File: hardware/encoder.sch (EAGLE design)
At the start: 10 parts, among them Q1 BCP56, Q2 BCP53, Q3 IRF540

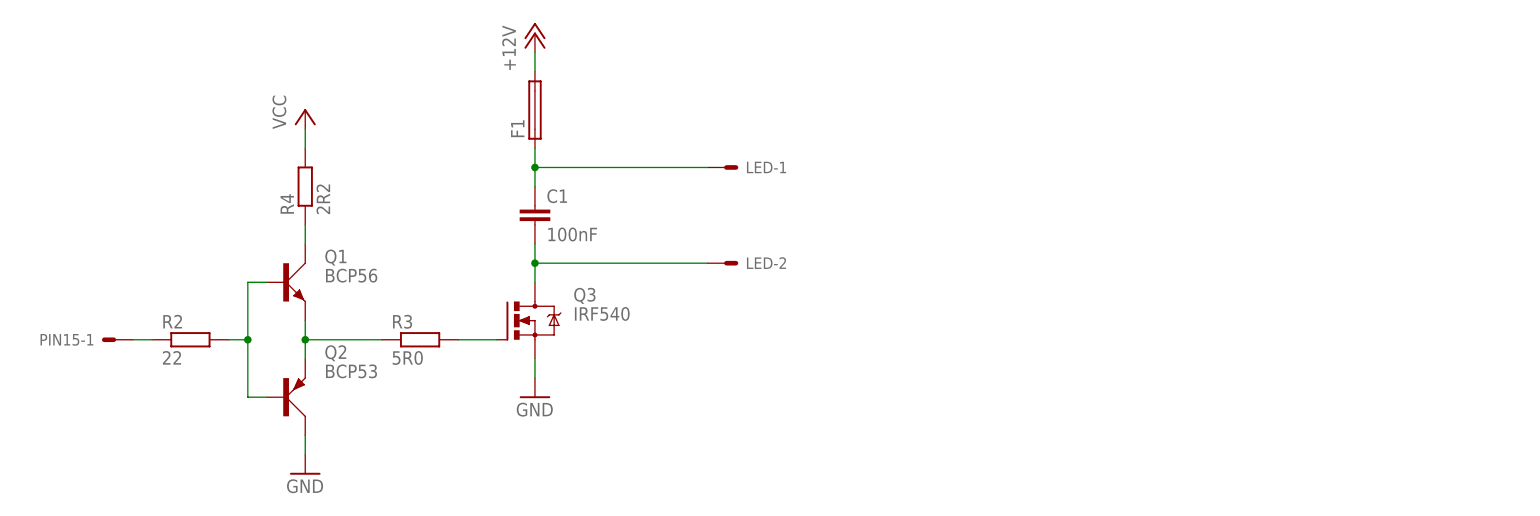
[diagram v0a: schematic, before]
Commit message: реорганизация
Разводка дочерней платы энкодера (теперь три платы в одном файле),
актуальная папка  для железа - hardware
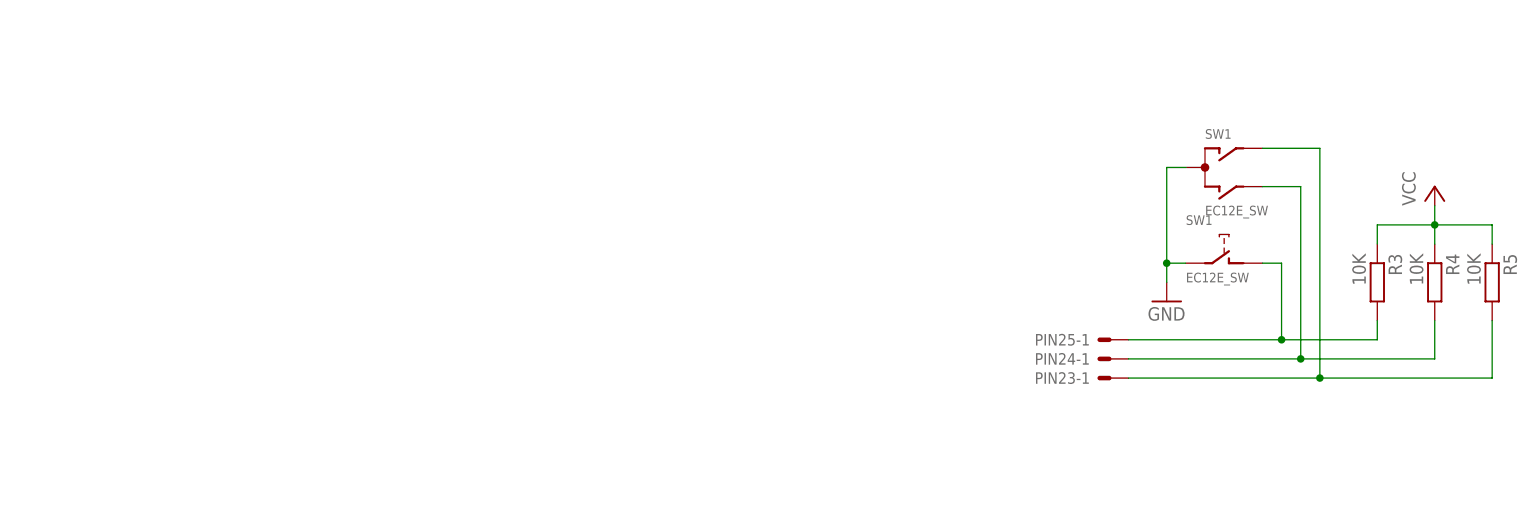
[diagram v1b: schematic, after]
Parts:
- removed C1: 100nF, capacitor-wima:C2,5-3
- removed F1: (no value), fuse:TE5
- removed LED, PIN15: 5566-10, con-molex:5566-10
- removed Q1: BCP56, transistor-small-signal:BC639
- removed Q2: BCP53, transistor-small-signal:BC640
- removed Q3: IRF540, transistor-power:IRF540
- removed R2: 22, resistor:R-EU_R1206
- added PIN23, PIN24, PIN25: 5566-10, con-molex:5566-10
- added R5: 10K, resistor:R-EU_M1206
- added SW1: EC12E_SW, switch-alps:EC12E_SW
- R3: value 5R0 -> 10K; device resistor:R-EU_R1206 -> resistor:R-EU_M1206
- R4: value 2R2 -> 10K; device resistor:R-EU_R1206 -> resistor:R-EU_M1206
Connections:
- removed net +12V: F1.2
- removed net N$12: Q1.C, R4.1
- removed net N$13: C1.1, F1.1, LED-1.S
- removed net N$6: PIN15-1.S, R2.1
- removed net N$8: Q1.E, Q2.E, R3.1
- net GND: now also SW1G$1.C, SW1G$2.2; no longer Q2.C, Q3.S
- net N$10: now also PIN25-1.S, R3.2, SW1G$2.1; no longer C1.2, LED-2.S, Q3.D
- net N$5: now also PIN23-1.S, R5.2, SW1G$1.A; no longer Q1.B, Q2.B, R2.2
- net N$9: now also PIN24-1.S, R4.2, SW1G$1.B; no longer Q3.G, R3.2
- net VCC: now also R3.1, R4.1, R5.1; no longer R4.2
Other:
- moved on the sheet: R3, R4
